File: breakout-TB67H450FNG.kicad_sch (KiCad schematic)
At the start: 8 parts, among them IC1 TB67H450FNG,EL, J1 Conn_01x06, J2 Screw_Terminal_01x02

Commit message: uploaded image to readme
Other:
- company: (none) -> Created by: Vincent Cayadi
- title: (none) -> Breakout TB67H450FNG
- moved on the sheet: C1, C2, C3, IC1, J2, R1, R2

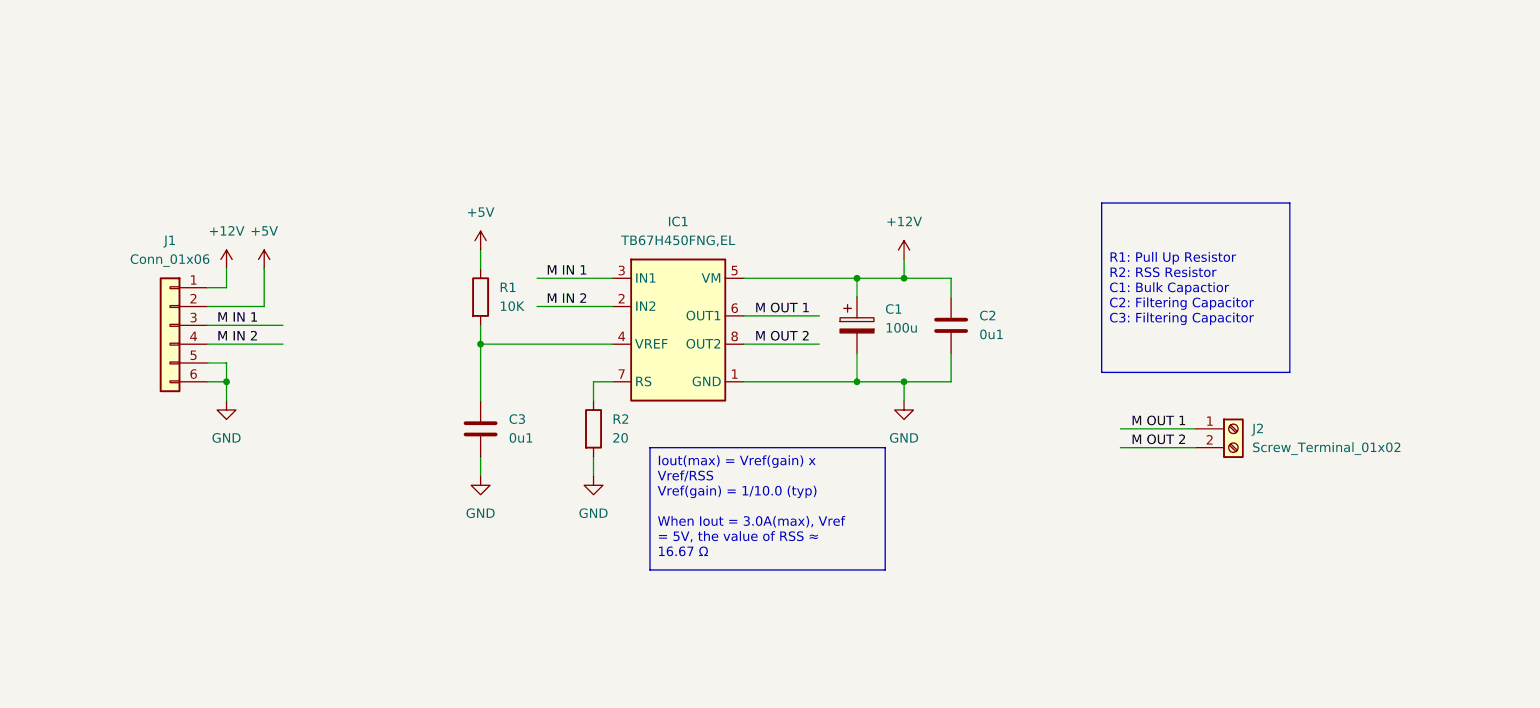
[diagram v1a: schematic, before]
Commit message: Changed Footpint, Added DEBUG LED, Layouted PCB
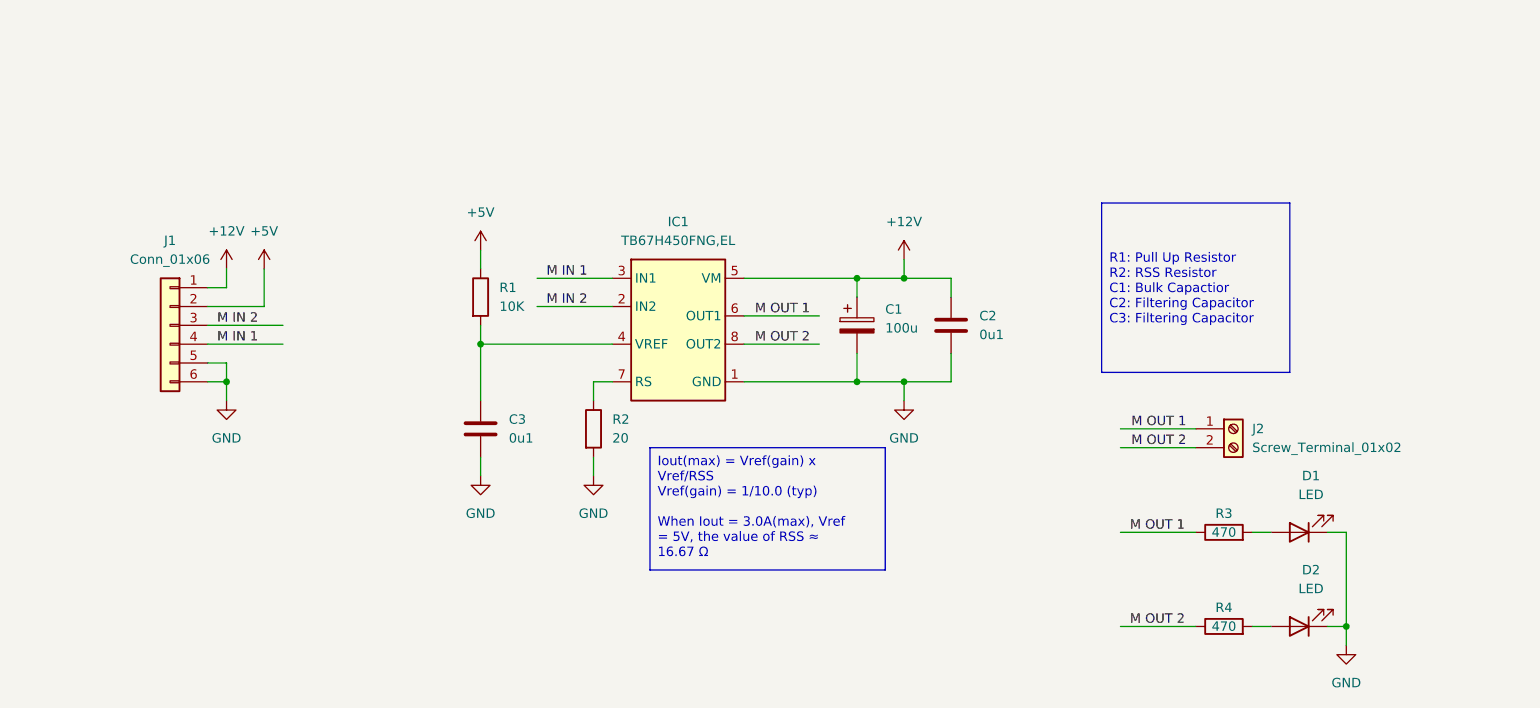
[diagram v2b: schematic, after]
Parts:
- added D1, D2: LED, breakout-TB67H450FNG:led0603, symbol Device:LED
- added R3, R4: 470, breakout-TB67H450FNG:res0603, symbol Device:R
- C1: footprint (none) -> breakout-TB67H450FNG:CP_Radial_D8.0mm_P3.50mm
- J1: footprint (none) -> Connector_PinSocket_2.54mm:PinSocket_1x06_P2.54mm_Vertical
- J2: footprint (none) -> breakout-TB67H450FNG:xt30-f
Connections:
- net GND: now also D1.1 (K), D2.1 (K)
- net M IN 1: now also J1.4 (Pin_4); no longer J1.3 (Pin_3)
- net M IN 2: now also J1.3 (Pin_3); no longer J1.4 (Pin_4)
- net M OUT 1: now also R3.1
- net M OUT 2: now also R4.1
- new net: D1.2 (A), R3.2
- new net: D2.2 (A), R4.2

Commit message: Almost close to finishing
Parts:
- added H1, H2, H3, H4: MountingHole_Pad, MountingHole:MountingHole_3.2mm_M3_Pad_Via, symbol Mechanical:MountingHole_Pad
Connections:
- net GND: now also H1.1, H2.1, H3.1, H4.1
